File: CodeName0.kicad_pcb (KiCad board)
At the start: 4 copper layers, 60 x 80 mm, 135 parts, among them J1 STM32 Debug Conn, J10 Telemetry 2 Conn, J11 I2C, J12 PWM Aux Conn, J2 Power Conn, J3 USB C 16p, J4 Telemetry 1 Conn, J5 MicroSD, J6 GPS Conn, J7 Buzzer Conn, J8 U.FL Hirose, J9 ESP32 Prog Conn, Q1 MMBT3904, SW1 Tactile Switch, SW2 Tactile Switch, SW3 Tactile Switch, SW4 Tactile Switch, U1 TPS5430DDAR, U2 AMS1117-3.3, U3 STM32H743VITx, U4 ICM-42688-P, U5 BMP388, U6 ESP32-C3FH4, U7 BCT4222CEAB-TR, U8 SX1280IMLTRT, Y1 X322525MOB4SI, Y2 X322540MPB4SI, Y3 OW7EL89CENUNFAYLC-52M

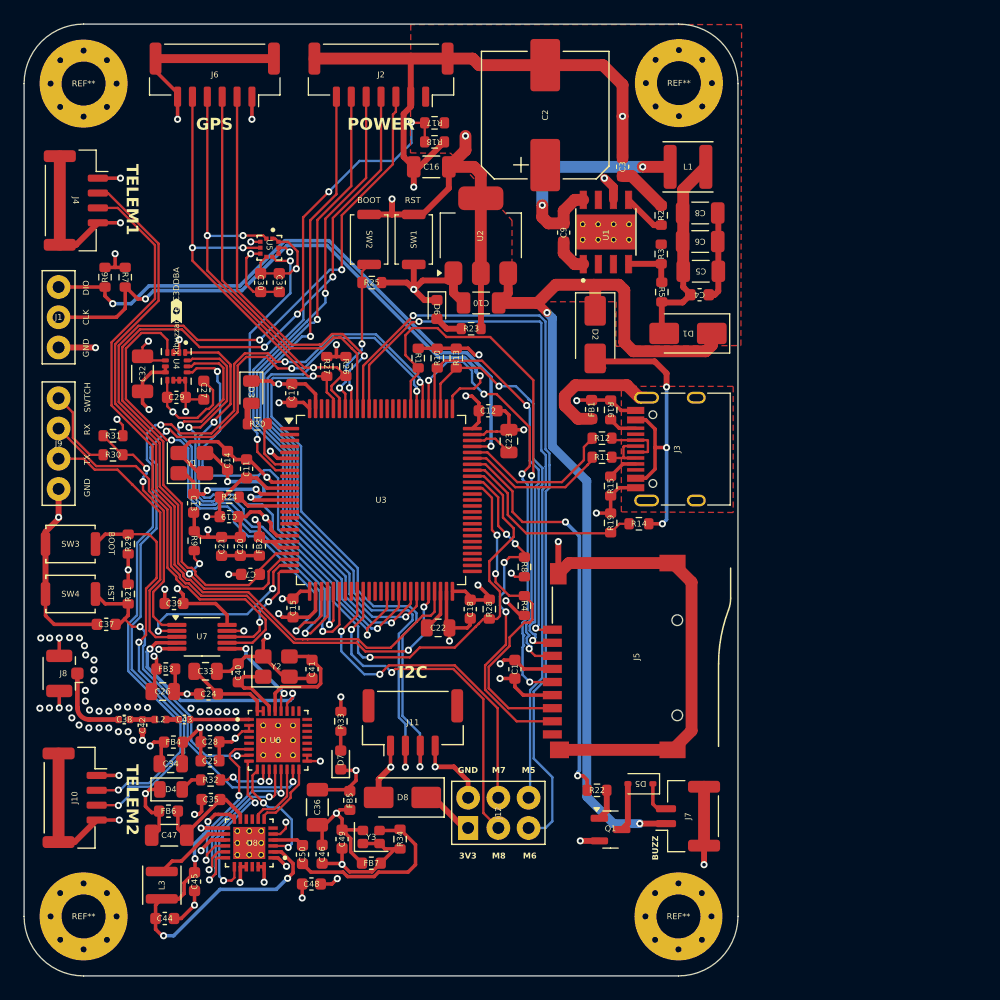
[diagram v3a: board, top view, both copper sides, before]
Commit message: feat: redesign power archtecture and integrate SX1280
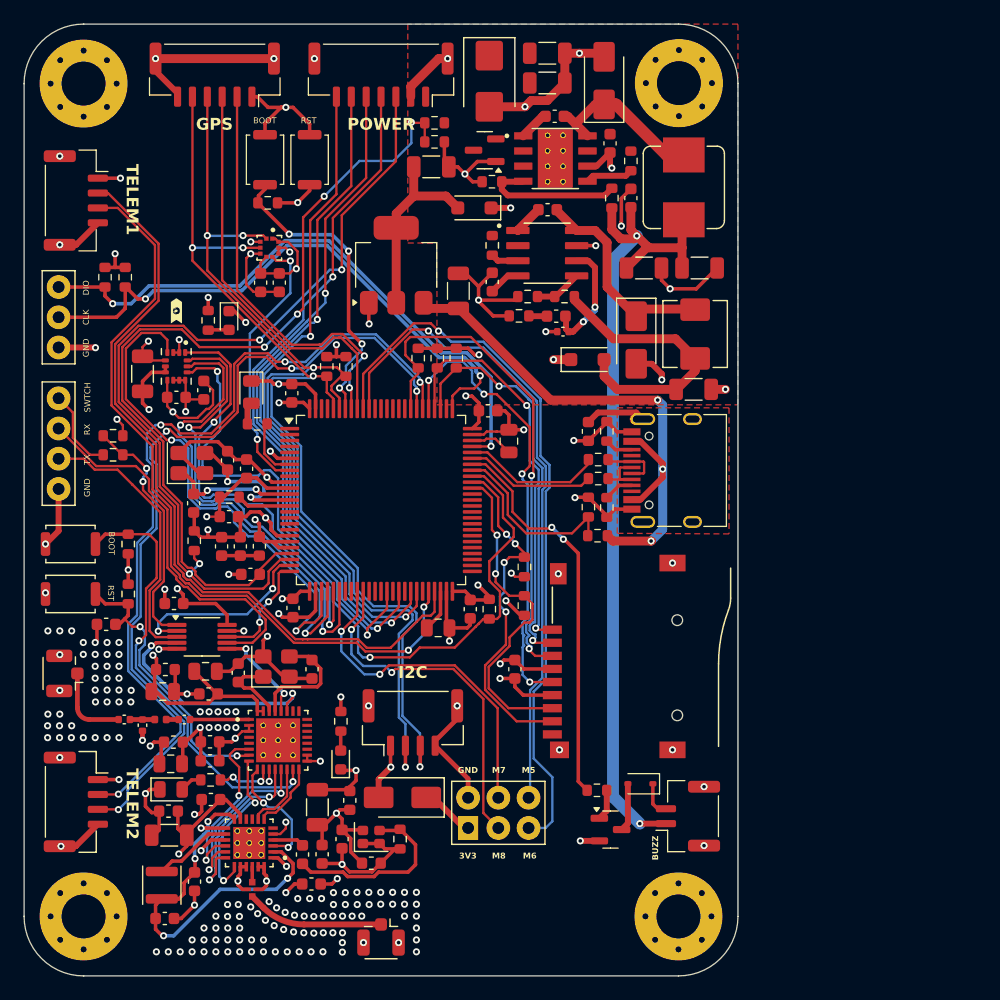
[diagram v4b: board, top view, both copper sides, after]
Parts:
- added C51: 100nF, Capacitor_SMD:C_0603_1608Metric, F.Cu at (144.0, 75.6)
- added C52: 47pF, Capacitor_SMD:C_0402_1005Metric, F.Cu at (145.3, 85.8)
- added C53: 1nF, Capacitor_SMD:C_0603_1608Metric, F.Cu at (144.7, 84.5)
- added C54: 100uF, Capacitor_SMD:C_1206_3216Metric, F.Cu at (156.8, 80.5)
- added C55: 100uF, Capacitor_SMD:C_1206_3216Metric, F.Cu at (156.3, 90.7)
- added D10: DSK34, Diode_SMD:D_SOD-123F, F.Cu at (137.8, 75.5)
- added D11: DSK34, Diode_SMD:D_SOD-123F, F.Cu at (147.3, 88.2)
- added D9: SS34, Diode_SMD:D_SMA, F.Cu at (151.4, 86.5)
- added FL1: 2450FM07D0034T, 2450FM07D0034T:FIL_2450FM07D0034T, F.Cu at (119.2, 132.7)
- added J13: U.FL Hirose, Connector_Coaxial:U.FL_Hirose_U.FL-R-SMT-1_Vertical, F.Cu at (130.0, 136.7)
- added L4: 6.8uH, Inductor_SMD:L_Sunlord_MWSA0503S, F.Cu at (156.4, 86.0)
- added Q2: AO3401A, Package_TO_SOT_SMD:SOT-23, F.Cu at (138.7, 70.6)
- added R35: 3.3K, Resistor_SMD:R_0603_1608Metric, F.Cu at (142.3, 82.9)
- added R36: 332K, Resistor_SMD:R_0603_1608Metric, F.Cu at (139.3, 78.6)
- added R37: 10K, Resistor_SMD:R_0603_1608Metric, F.Cu at (145.4, 82.9)
- added R38: 30K, Resistor_SMD:R_0603_1608Metric, F.Cu at (141.6, 84.5)
- added U9: TPS54331DR, TPS54331DR:SOIC127P599X175-8N, F.Cu at (144.0, 79.3)
- C2: value 470uF -> 22uF; footprint Capacitor_SMD:CP_Elec_10x10.5 -> Capacitor_SMD:C_1206_3216Metric
- C6: value 22uF -> 100uF
- C8: value 22uF -> 100nF; footprint Capacitor_SMD:C_1206_3216Metric -> Capacitor_SMD:C_0603_1608Metric
- C9: value 10nF -> 100nF
- D1: value SS34 -> SMBJ15A; footprint Diode_SMD:D_SMA -> Diode_SMD:D_SMB
- L1: footprint Inductor_SMD:L_Changjiang_FNR4020S -> Inductor_SMD:L_Bourns_SRP7028A_7.3x6.6mm
- R3: value 10K -> 3.3K
- R5: value 30.9K -> 10K
- moved D1 27.0 mm to (139.1, 64.8), turned to -90 degrees
- moved C5 22.4 mm to (144.0, 62.5)
- moved R23 22.1 mm to (115.5, 84.9), turned to 90 degrees
- moved D2 21.4 mm to (148.8, 64.8), turned to 90 degrees
- moved C8 18.4 mm to (139.3, 81.7), turned to 90 degrees
- moved D6 17.5 mm to (117.2, 84.9)
- moved R3 15.5 mm to (139.3, 73.2), turned to 0 degrees
- moved R25 11.0 mm to (120.5, 75.0)
- moved SW1 11.0 mm to (124.0, 71.4)
- moved SW2 11.0 mm to (120.2, 71.4)
- moved C4 9.97 mm to (151.0, 74.6), turned to 90 degrees
- moved C9 9.80 mm to (144.6, 67.8), turned to 0 degrees
- moved R5 8.95 mm to (149.4, 74.6)
- moved U2 7.53 mm to (131.3, 80.3)
- moved U1 7.50 mm to (144.7, 71.3), turned to 0 degrees
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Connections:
- C16 pad 1: +3.3V -> Net-(D10-A)
- C4 pad 1: Net-(D1-A) -> +5V
- C5 pad 1: Net-(D1-A) -> +BATT
- C6 pad 1: Net-(D1-A) -> +5V
- C8 pad 1: Net-(D1-A) -> Net-(U9-SS)
- C9 pad 2: Net-(U1-PH) -> Net-(D2-K)
- D1 pad 1: +5V -> +BATT
- D1 pad 2: Net-(D1-A) -> GND
- D2 pad 1: +5V -> Net-(D2-K)
- D2 pad 2: Net-(D2-A) -> GND
- J10 pad MP: (no net) -> GND
- J11 pad MP: (no net) -> GND
- J2 pad MP: (no net) -> GND
- J3 pad A4: Net-(D2-A) -> +5V
- J3 pad A9: Net-(D2-A) -> +5V
- J3 pad B4: Net-(D2-A) -> +5V
- J3 pad B9: Net-(D2-A) -> +5V
- J4 pad MP: (no net) -> GND
- J6 pad MP: (no net) -> GND
- J7 pad MP: (no net) -> GND
- L1 pad 1: Net-(U1-PH) -> +5V
- L1 pad 2: Net-(D1-A) -> Net-(D2-K)
- R14 pad 2: Net-(D2-A) -> +5V
- R5 pad 1: Net-(D1-A) -> +5V
- U1 pad 8: Net-(U1-PH) -> Net-(D2-K)
- U2 pad 2: +3.3V -> Net-(D10-A)
- U8 pad 22: unconnected-(U8-RFIO-Pad22) -> SX_RFIO
- U8 pad 25: unconnected-(U8-EXP-Pad25) -> GND
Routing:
- net GND: track 342.1 -> 260.2 mm, vias 89 -> 198
- net +5V: track 80.5 -> 118.2 mm, vias 2 -> 5
- net Net-(D2-A): track 30.2 -> 0.00 mm, vias 3 -> 0
- net Net-(D11-A): track 0.00 -> 23.7 mm
- net Net-(U1-PH): track 19.6 -> 0.00 mm, vias 2 -> 0
- net Net-(D9-K): track 0.00 -> 17.7 mm
- net Net-(D1-A): track 17.2 -> 0.00 mm
- net Net-(D10-A): track 0.00 -> 16.2 mm
- net Net-(D2-K): track 0.00 -> 14.2 mm
- net +3.3V: track 172.2 -> 159.6 mm, vias 34 -> 36
- net BOOT0: track 13.5 -> 25.7 mm, vias 2 -> 4
- net Net-(J13-In): track 0.00 -> 11.6 mm
- net Net-(U9-COMP): track 0.00 -> 9.67 mm, vias 0 -> 2
- net Net-(U1-VSENSE): track 4.33 -> 12.1 mm
- net SHIELD: track 11.2 -> 5.73 mm
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
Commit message: feat: polishing and finishing
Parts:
- added C56: 100uF, Capacitor_SMD:C_1206_3216Metric, F.Cu at (158.9, 128.1)
- added D12: LED, LED_SMD:LED_0603_1608Metric, F.Cu at (164.9, 126.0)
- added R39: 330, Resistor_SMD:R_0603_1608Metric, F.Cu at (164.9, 124.3)
- added TP1: TestPoint, TestPoint:TestPoint_Pad_D1.5mm, F.Cu at (162.6, 87.3)
- added TP3: TestPoint, TestPoint:TestPoint_Pad_D1.5mm, F.Cu at (156.7, 78.3)
- added TP4: TestPoint, TestPoint:TestPoint_Pad_D2.5mm, F.Cu at (130.7, 69.5)
- added TP5: TestPoint, TestPoint:TestPoint_Pad_D1.5mm, F.Cu at (159.8, 119.7)
- added TP6: TestPoint, TestPoint:TestPoint_Pad_D1.5mm, F.Cu at (165.0, 93.3)
- added TP7: TestPoint, TestPoint:TestPoint_Pad_D1.5mm, F.Cu at (127.5, 99.8)
- D8: value SS34 -> DSK34; footprint Diode_SMD:D_SMA -> Diode_SMD:D_SOD-123F
- J12: value PWM Aux Conn -> AUX Motor Pin; footprint Connector_PinHeader_2.54mm:PinHeader_2x03_P2.54mm_Vertical -> Library:PinHeader_3x04_P2.54mm_Vertical
- R3, R35: value 3.3K -> 2.7K
- moved D8 32.0 mm to (163.6, 128.1), turned to 0 degrees
- moved J12 24.2 mm to (165.8, 131.2)
- moved C20 20.0 mm to (138.2, 103.9)
- moved C32 20.0 mm to (130.0, 89.4)
- moved C46 20.0 mm to (145.1, 129.8)
- moved D7 20.0 mm to (146.6, 121.8)
- moved FB4 20.0 mm to (132.6, 120.3)
- moved FL1 20.0 mm to (139.2, 132.7)
- moved R26 20.0 mm to (147.1, 88.8)
- moved R32 20.0 mm to (135.7, 123.5)
- moved R9 20.0 mm to (134.3, 103.4)
- moved U5 20.0 mm to (140.6, 78.8)
- moved U8 20.0 mm to (138.9, 128.8)
- moved kibuzzard-68C3DDBA 20.0 mm to (132.8, 84.1)
- moved C1 20.0 mm to (161.2, 114.2)
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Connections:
- C10 pad 1: +5V -> +5V_USB
- D8 pad 1: Net-(D8-K) -> +5V
- D8 pad 2: +3.3V -> GND
- J12 pad 2: TIM3_CH2 -> +5V
- J12 pad 3: TIM3_CH3 -> GND
- J12 pad 4: TIM3_CH4 -> TIM3_CH2
- J12 pad 5: GND -> +5V
- J12 pad 6: Net-(D8-K) -> GND
- J3 pad A4: +5V -> +5V_USB
- J3 pad A9: +5V -> +5V_USB
- J3 pad B4: +5V -> +5V_USB
- J3 pad B9: +5V -> +5V_USB
- R14 pad 2: +5V -> +5V_USB
- U2 pad 3: +5V -> +5V_USB
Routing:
- net +5V_USB: track 0.00 -> 49.0 mm, vias 0 -> 3
- net GND: track 260.2 -> 308.0 mm, vias 198 -> 219
- net +5V: track 118.2 -> 90.5 mm
- net TIM3_CH3: track 28.8 -> 38.6 mm
- net TIM3_CH1: track 55.2 -> 63.6 mm, vias 1 -> 2
- net Net-(D11-A): track 23.7 -> 30.7 mm
- net TIM3_CH2: track 61.5 -> 67.4 mm, vias 1 -> 2
- net TIM3_CH4: track 30.0 -> 34.8 mm
- net Net-(D8-K): track 3.63 -> 0.00 mm
- net Net-(D2-K): track 14.2 -> 17.6 mm, vias 0 -> 2
- net Net-(D12-A): track 0.00 -> 1.66 mm
- net +3.3V: track 159.6 -> 158.4 mm, vias 36 -> 37
- net SDMMC_DAT0: track 28.1 -> 27.5 mm
- added copper zone on F.Cu, net +5V
- added copper zone on B.Cu, net GND
- added copper zone on F.Cu, net GND
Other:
- board text removed: "3V3"
- board text removed: "M5"
- board text removed: "M6"
- board text removed: "M7"
- board text removed: "M8"
